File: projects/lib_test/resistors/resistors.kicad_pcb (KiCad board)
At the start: 2 copper layers, 125 x 45 mm, 170 parts

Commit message: updated test projects
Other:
- board size 125 x 45 mm -> 122 x 44 mm
- board text added: "RESISTORS 0805"

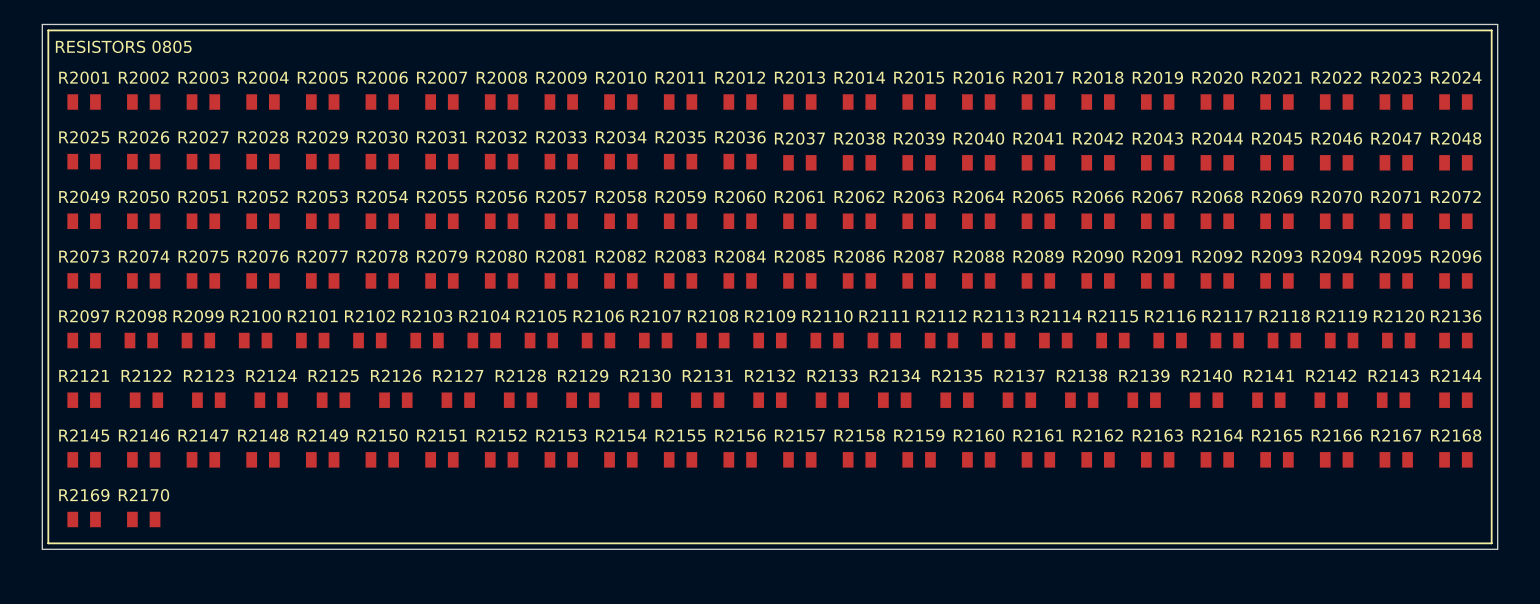
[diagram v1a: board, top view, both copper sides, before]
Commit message: updated resistors test design
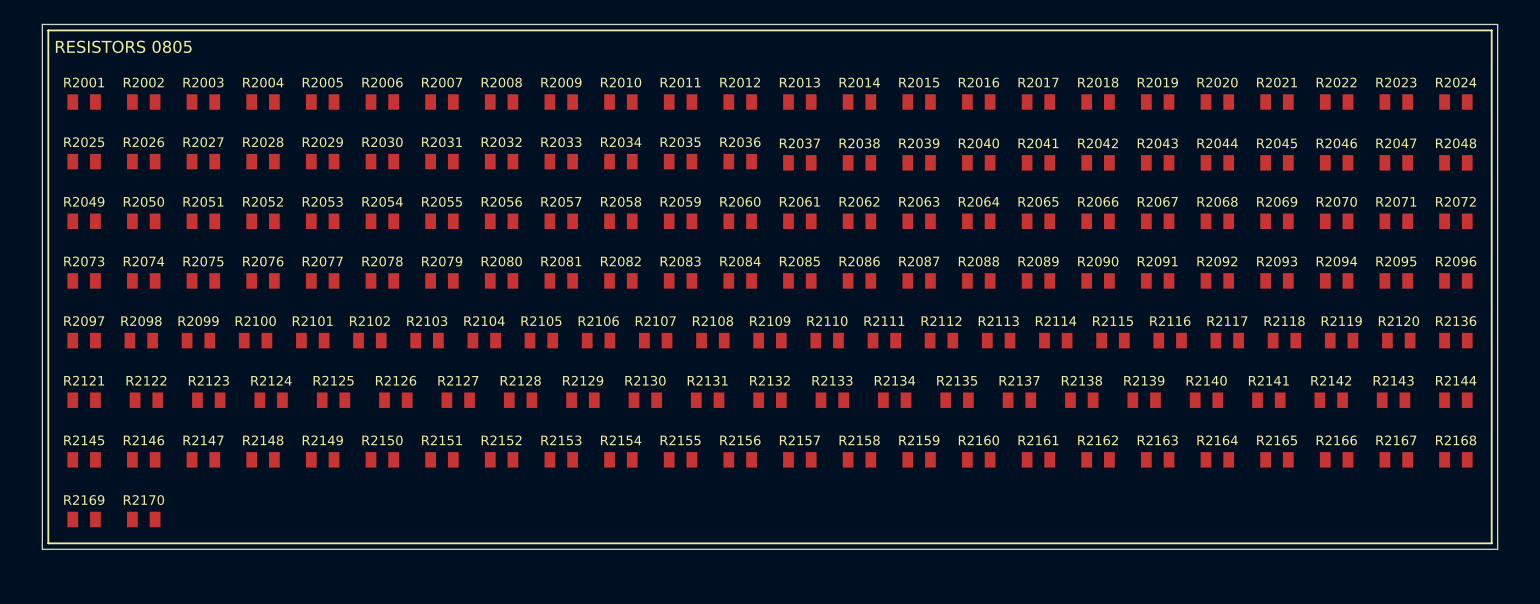
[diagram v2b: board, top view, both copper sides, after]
